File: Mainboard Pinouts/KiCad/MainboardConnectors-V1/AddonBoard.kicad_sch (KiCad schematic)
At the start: 8 parts, among them M1 Fan_External(40mm), M2 Fan_Recirculating, Q1 IRLZ44N

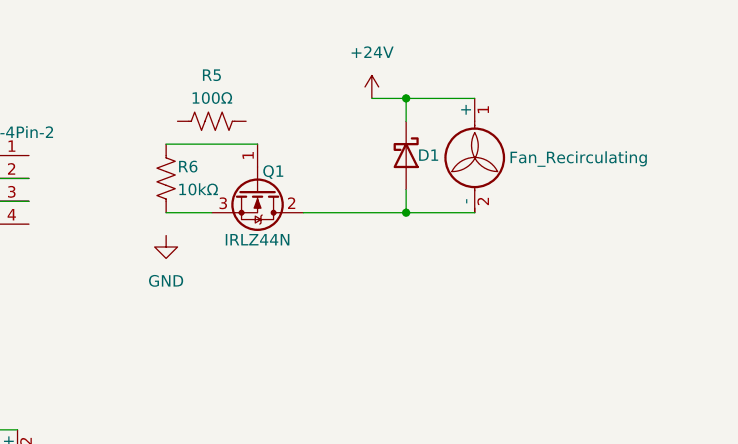
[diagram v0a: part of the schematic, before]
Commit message: Added ferrite bead
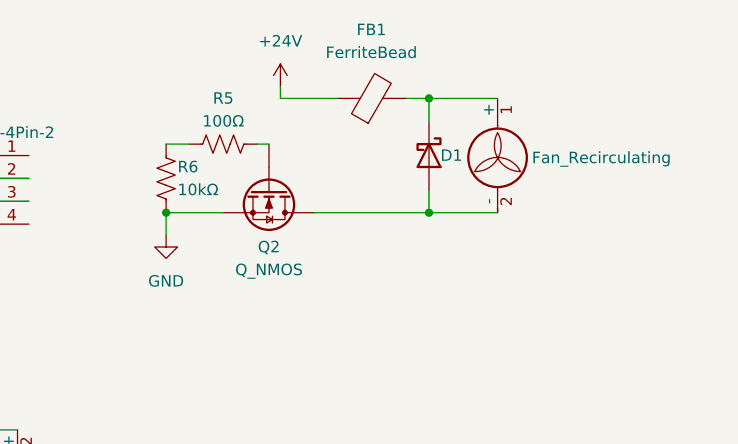
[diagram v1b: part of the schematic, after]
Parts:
- removed Q1: IRLZ44N, Package_TO_SOT_THT:TO-220-3_Vertical, symbol Transistor_FET:IRLZ44N
- added FB1: FerriteBead, symbol Device:FerriteBead
- added Q2: Q_NMOS, symbol Device:Q_NMOS
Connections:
- net +24V: now also FB1.1; no longer D1.1 (K), M2.1 (+)
- net GND: now also R6.2, Q2.S
- net at R6.1: now also R5.1
- net at D1.2 (A), M2.2 (-): now also Q2.D
- net at R5.2: now also Q2.G
- new net: D1.1 (K), FB1.2, M2.1 (+)
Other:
- moved on the sheet: D1, R5

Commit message: Finished V1 build of addon board
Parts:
- added D2, D3: D_Schottky, symbol Device:D_Schottky
- added J1: PB8 Pad, symbol Connector:Conn_01x01_Pin
- added J2, J3: Conn_01x04, symbol Connector_Generic:Conn_01x04
- added J4: Conn_01x03, symbol Connector_Generic:Conn_01x03
- added J5: Conn_01x02_Pin, symbol Connector:Conn_01x02_Pin
- added J6: PB6 Pad, symbol Connector:Conn_01x01_Pin
- added M3: Fan_External(40mm), symbol Motor:Fan_4pin
- added Q1, Q3: IRLZ44N, Package_TO_SOT_THT:TO-220-3_Vertical, symbol Transistor_FET:IRLZ44N
- added R10, R9: 10kΩ, symbol Device:R_US
- added R11, R12: 47Ω, symbol Device:R_US
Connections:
- net +24V: now also D3.1 (K), J4.3 (Pin_3), J5.2 (Pin_2)
- net GND: now also JSTXH-4Pin-2.1 (Pin_1), J4.1 (Pin_1), Q1.3 (S), Q3.3 (S)
- net PA13: now also R12.1
- net PA14: now also R11.1
- net +3.3V: now reaches JSTXH-4Pin-2.4 (Pin_4)
- net +3.3V: now also R10.1, R9.1
- new net: J2.2 (Pin_2), R10.2, R11.2
- new net: J1.1 (Pin_1), Q3.1 (G)
- new net: D3.2 (A), J5.1 (Pin_1), Q3.2 (D)
- new net: J2.1 (Pin_1), R12.2, R9.2
- new net: D2.2 (A), J2.4 (Pin_4), Q1.2 (D)
- new net: J3.1 (Pin_1), M3.1 (-)
- new net: J3.2 (Pin_2), M3.2 (+)
- new net: J3.3 (Pin_3), M3.3 (Tacho)
- new net: J3.4 (Pin_4), M3.4 (PWM)
- new net: J6.1 (Pin_1), Q1.1 (G)
- new net +12V: D2.1 (K), J2.3 (Pin_3), J4.2 (Pin_2)
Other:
- note added: "Built-in Pullups on PCB"
- note added: "Connector to 12V Buck"
- note added: "SWD Port"
- note added: "Simple 24V Fan #1"
- moved on the sheet: D1, FB1, JSTXH-4Pin-1, JSTXH-4Pin-2, Q2, R5, R6

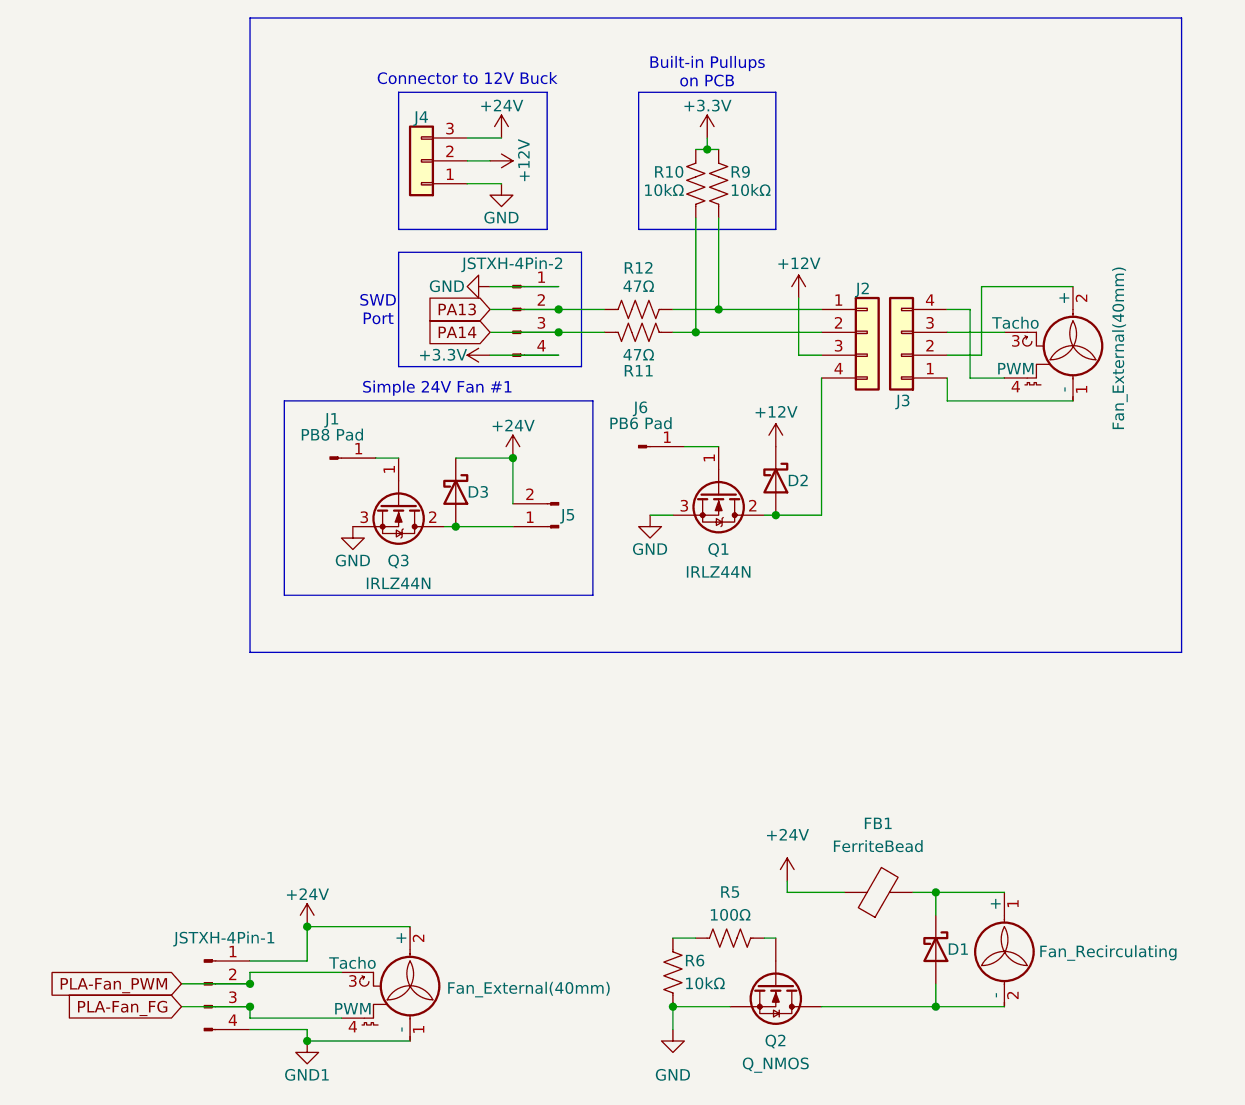
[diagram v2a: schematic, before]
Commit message: Finished Perfboard Design
Finished schematic for the Add-On board that was made on perfboard. Need to create Mk2 for PCB design.
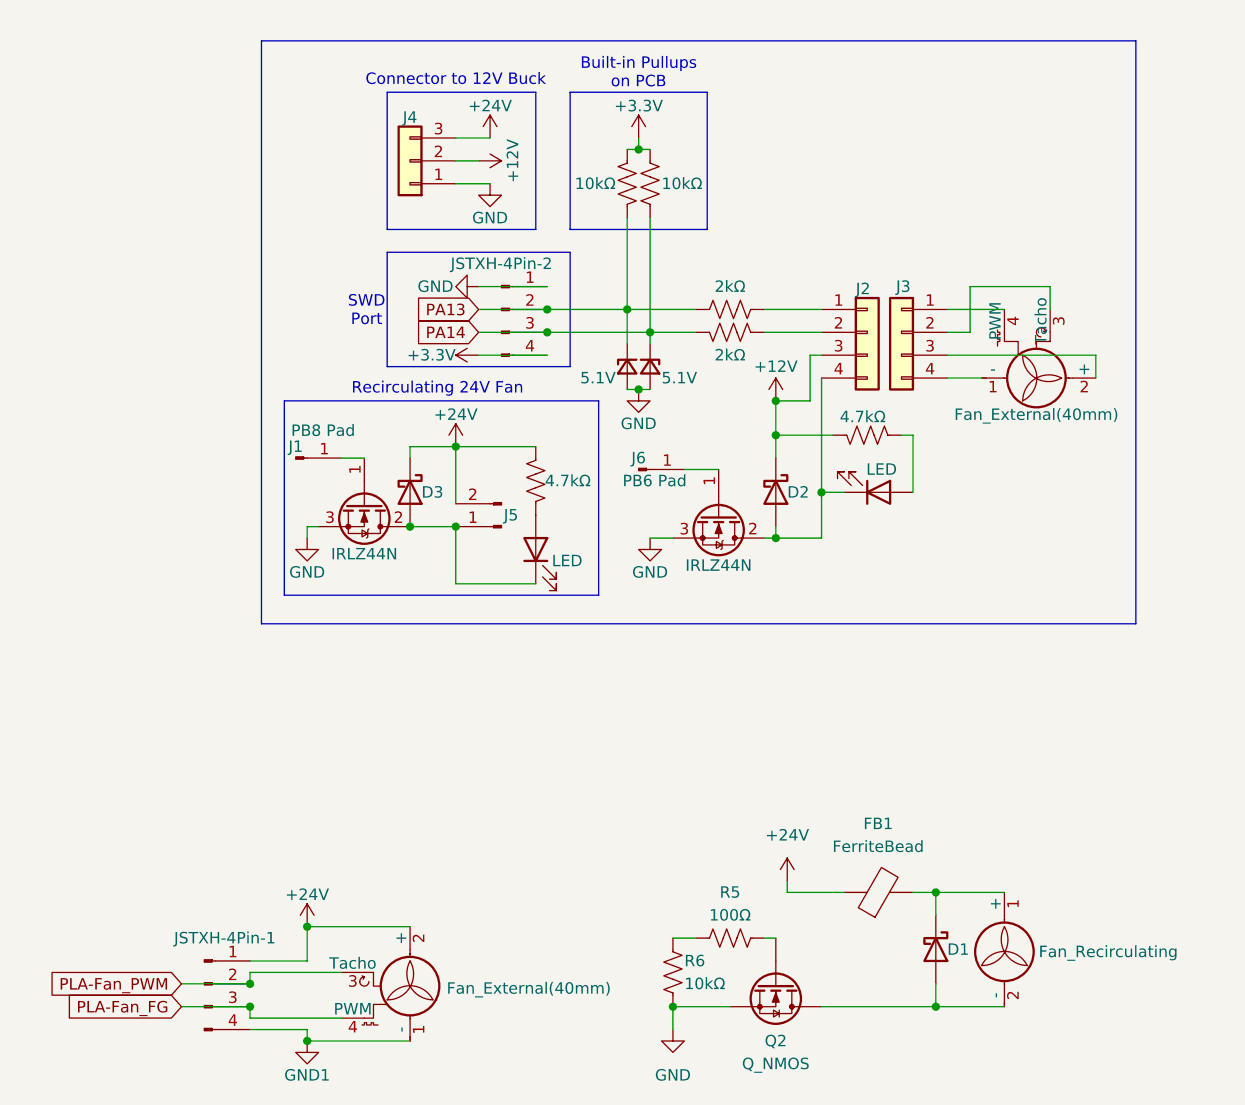
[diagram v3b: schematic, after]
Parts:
- added D4, D5: LED, symbol Device:LED
- added D8, D9: 5.1V, symbol Device:D_Zener_Small
- added R13, R14: 4.7kΩ, symbol Device:R_US
- R11, R12: value 47Ω -> 2kΩ
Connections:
- net +12V: now also R14.2
- net +24V: now also R13.2
- net GND: now also D8.2 (A), D9.2 (A)
- net PA13: now also R10.2, D9.1 (K)
- net PA14: now also R9.2, D8.1 (K)
- net at J2.2 (Pin_2), R11.2: no longer R10.2
- net at D3.2 (A), J5.1 (Pin_1), Q3.2 (D): now also D4.1 (K)
- net at J2.1 (Pin_1), R12.2: no longer R9.2
- net at D2.2 (A), J2.4 (Pin_4), Q1.2 (D): now also D5.1 (K)
- net at M3.1 (-): now also J3.4 (Pin_4); no longer J3.1 (Pin_1)
- net at M3.2 (+): now also J3.3 (Pin_3); no longer J3.2 (Pin_2)
- net at M3.3 (Tacho): now also J3.2 (Pin_2); no longer J3.3 (Pin_3)
- net at M3.4 (PWM): now also J3.1 (Pin_1); no longer J3.4 (Pin_4)
- new net: D4.2 (A), R13.1
- new net: D5.2 (A), R14.1
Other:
- note added: "Recirculating 24V Fan"
- note removed: "Simple 24V Fan #1"
- moved on the sheet: D2, D3, J1, J3, J4, J5, J6, JSTXH-4Pin-2
